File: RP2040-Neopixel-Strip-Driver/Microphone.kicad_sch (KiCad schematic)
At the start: 0 parts

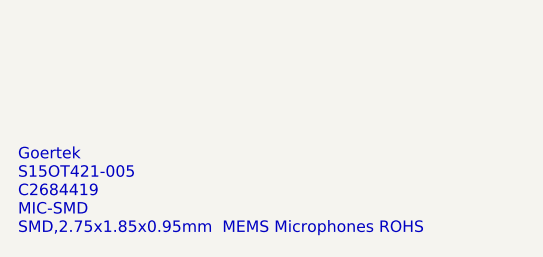
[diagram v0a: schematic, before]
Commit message: Made microphone symbol, footprint, and 3D model.
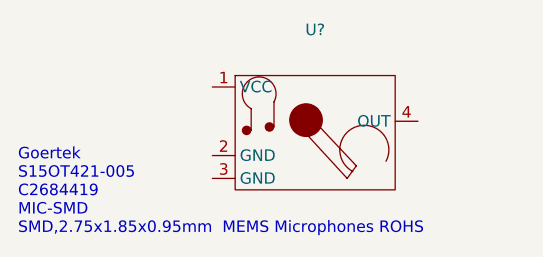
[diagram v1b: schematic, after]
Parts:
- added U?: (no value), symbol BreadstickLibrary:S15OT421-005
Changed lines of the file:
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@@
     (effects (font (size 1.27 1.27)) (justify left bottom))
   )
+  (symbol (lib_id "BreadstickLibrary:S15OT421-005") (at 88.9 142.24 0) (unit 1)
+    (in_bom yes) (on_board yes) (fields_autoplaced)
+    (property "Reference" "U?" (id 0) (at 87.63 132.08 0))
+    (property "Value" "" (id 1) (at 87.63 134.62 0))
+    (property "Footprint" "" (id 2) (at 78.74 138.43 0)
+      (effects (font (size 1.27 1.27)) hide)
+    )
+    (property "Datasheet" "" (id 3) (at 78.74 138.43 0)
+      (effects (font (size 1.27 1.27)) hide)
+    )
+    (pin "1")
+    (pin "2")
+    (pin "3")
+    (pin "4")
+  )
 )

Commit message: Added Motor Driver
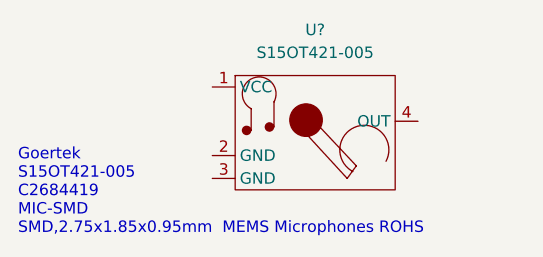
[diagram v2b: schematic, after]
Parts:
- U?: value (none) -> S15OT421-005
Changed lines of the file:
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@@
     (in_bom yes) (on_board yes) (fields_autoplaced)
     (property "Reference" "U?" (id 0) (at 87.63 132.08 0))
-    (property "Value" "" (id 1) (at 87.63 134.62 0))
+    (property "Value" "S15OT421-005" (id 1) (at 87.63 134.62 0))
     (property "Footprint" "" (id 2) (at 78.74 138.43 0)
       (effects (font (size 1.27 1.27)) hide)

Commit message: Updated all IC symbols to have filled background, personal preference.
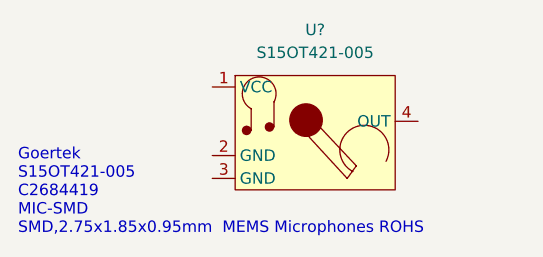
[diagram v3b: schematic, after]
